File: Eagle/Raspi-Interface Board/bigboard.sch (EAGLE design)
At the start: 25 parts, among them M1 SMALL_SERVO, M2 SMALL_SERVO, M3 SMALL_SERVO, M4 SMALL_SERVO, M5 SMALL_SERVO, U1 ATMEGA328P-AU

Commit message: AVR ISP pins corrected
In the R1 of the board the AVR ISP pins were totally attached to the
wrong. 13 != 3. Double check work done at 4AM next time.
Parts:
- removed IC1, IC2: (no value), RepRapjr:78LXXLM78L05ACZ
- added 3VREG, 5VREG: (no value), SparkFun-Connectors:M03PTH
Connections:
- net 3V: now also 3VREG.1; no longer IC2.OUT
- net 5V: now also 3VREG.3, 5VREG.1; no longer IC1.OUT, IC2.IN
- net A3: now also JP3.4
- net A4: no longer JP3.4
- net ATX: no longer ISP1.MISO
- net D12: now also ISP1.MISO
- net D13: now also ISP1.SCK
- net D3: no longer ISP1.SCK
- net GND: now also 3VREG.2, 5VREG.2; no longer IC1.GND, IC2.GND
- net VIN: now also 5VREG.3; no longer IC1.IN
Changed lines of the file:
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@@
 <part name="M4" library="SparkFun-Electromechanical" deviceset="SMALL_SERVO" device=""/>
 <part name="M5" library="SparkFun-Electromechanical" deviceset="SMALL_SERVO" device=""/>
-<part name="IC1" library="RepRapjr" deviceset="78LXX" device="LM78L05ACZ"/>
-<part name="IC2" library="RepRapjr" deviceset="78LXX" device="LM78L05ACZ"/>
 <part name="Y1" library="SparkFun-FreqCtrl" deviceset="RESONATOR" device="PTH"/>
 <part name="D1" library="SparkFun-LED" deviceset="LED-BLUE" device="0603" value="BLUE"/>
@@
 <part name="JP4" library="SparkFun-Connectors" deviceset="M07" device=""/>
 <part name="ISP1" library="adafruit" deviceset="AVRISP" device="-6"/>
+<part name="5VREG" library="SparkFun-Connectors" deviceset="M03" device="PTH"/>
+<part name="3VREG" library="SparkFun-Connectors" deviceset="M03" device="PTH"/>
 </parts>
 <sheets>
@@
 <instance part="M4" gate="G$1" x="309.88" y="71.12"/>
 <instance part="M5" gate="G$1" x="309.88" y="48.26"/>
-<instance part="IC1" gate="1" x="172.72" y="167.64"/>
-<instance part="IC2" gate="1" x="134.62" y="167.64"/>
 <instance part="Y1" gate="G$1" x="132.08" y="124.46"/>
 <instance part="D1" gate="G$1" x="170.18" y="231.14"/>
@@
 <instance part="JP4" gate="G$1" x="127" y="-43.18"/>
 <instance part="ISP1" gate="G$1" x="162.56" y="93.98"/>
+<instance part="5VREG" gate="G$1" x="109.22" y="177.8"/>
+<instance part="3VREG" gate="G$1" x="109.22" y="160.02"/>
 </instances>
 <busses>
@@
 <wire x1="132.08" y1="-35.56" x2="134.62" y2="-35.56" width="0.1524" layer="91"/>
 </segment>
+<segment>
+<pinref part="ISP1" gate="G$1" pin="MISO"/>
+<wire x1="149.86" y1="96.52" x2="147.32" y2="96.52" width="0.1524" layer="91"/>
+</segment>
 </net>
 <net name="D13" class="0">
@@
 <wire x1="132.08" y1="-33.02" x2="134.62" y2="-33.02" width="0.1524" layer="91"/>
 </segment>
+<segment>
+<pinref part="ISP1" gate="G$1" pin="SCK"/>
+<wire x1="149.86" y1="93.98" x2="147.32" y2="93.98" width="0.1524" layer="91"/>
+</segment>
 </net>
 <net name="XTAL1" class="0">
@@
 <wire x1="134.62" y1="66.04" x2="139.7" y2="66.04" width="0.1524" layer="91"/>
 </segment>
+<segment>
+<pinref part="JP3" gate="G$1" pin="4"/>
+<wire x1="88.9" y1="-40.64" x2="91.44" y2="-40.64" width="0.1524" layer="91"/>
+</segment>
 </net>
 <net name="A4" class="0">
@@
 <pinref part="U1" gate="A" pin="PC4"/>
 <wire x1="134.62" y1="63.5" x2="139.7" y2="63.5" width="0.1524" layer="91"/>
-</segment>
-<segment>
-<pinref part="JP3" gate="G$1" pin="4"/>
-<wire x1="88.9" y1="-40.64" x2="91.44" y2="-40.64" width="0.1524" layer="91"/>
 </segment>
 <segment>
@@
 <junction x="83.82" y="137.16"/>
 </segment>
-<segment>
-<pinref part="ISP1" gate="G$1" pin="MISO"/>
-<wire x1="149.86" y1="96.52" x2="147.32" y2="96.52" width="0.1524" layer="91"/>
-</segment>
 </net>
 <net name="D2" class="0">
@@
 <wire x1="312.42" y1="119.38" x2="317.5" y2="119.38" width="0.1524" layer="91"/>
 </segment>
-<segment>
-<pinref part="ISP1" gate="G$1" pin="SCK"/>
-<wire x1="149.86" y1="93.98" x2="147.32" y2="93.98" width="0.1524" layer="91"/>
-</segment>
 </net>
 <net name="D4" class="0">
@@
 </segment>
 <segment>
-<pinref part="IC1" gate="1" pin="IN"/>
-<wire x1="165.1" y1="167.64" x2="162.56" y2="167.64" width="0.1524" layer="91"/>
+<pinref part="5VREG" gate="G$1" pin="3"/>
+<wire x1="116.84" y1="180.34" x2="119.38" y2="180.34" width="0.1524" layer="91"/>
 </segment>
 </net>
@@
 </segment>
 <segment>
-<pinref part="IC1" gate="1" pin="GND"/>
-<wire x1="172.72" y1="160.02" x2="172.72" y2="157.48" width="0.1524" layer="91"/>
-</segment>
-<segment>
-<pinref part="IC2" gate="1" pin="GND"/>
-<wire x1="134.62" y1="160.02" x2="134.62" y2="157.48" width="0.1524" layer="91"/>
-</segment>
-<segment>
 <pinref part="Y1" gate="G$1" pin="2"/>
 <wire x1="132.08" y1="116.84" x2="132.08" y2="114.3" width="0.1524" layer="91"/>
@@
 <pinref part="ISP1" gate="G$1" pin="GND"/>
 <wire x1="177.8" y1="91.44" x2="180.34" y2="91.44" width="0.1524" layer="91"/>
+</segment>
+<segment>
+<pinref part="5VREG" gate="G$1" pin="2"/>
+<wire x1="116.84" y1="177.8" x2="119.38" y2="177.8" width="0.1524" layer="91"/>
+</segment>
+<segment>
+<pinref part="3VREG" gate="G$1" pin="2"/>
+<wire x1="116.84" y1="160.02" x2="119.38" y2="160.02" width="0.1524" layer="91"/>
 </segment>
 </net>
@@
 </segment>
 <segment>
-<pinref part="IC1" gate="1" pin="OUT"/>
-<wire x1="180.34" y1="167.64" x2="182.88" y2="167.64" width="0.1524" layer="91"/>
-</segment>
-<segment>
-<pinref part="IC2" gate="1" pin="IN"/>
-<wire x1="127" y1="167.64" x2="124.46" y2="167.64" width="0.1524" layer="91"/>
-</segment>
-<segment>
 <pinref part="ISP1" gate="G$1" pin="VCC"/>
 <wire x1="177.8" y1="96.52" x2="180.34" y2="96.52" width="0.1524" layer="91"/>
@@
 <wire x1="38.1" y1="71.12" x2="35.56" y2="71.12" width="0.1524" layer="91"/>
 </segment>
+<segment>
+<pinref part="5VREG" gate="G$1" pin="1"/>
+<wire x1="116.84" y1="175.26" x2="119.38" y2="175.26" width="0.1524" layer="91"/>
+</segment>
+<segment>
+<pinref part="3VREG" gate="G$1" pin="3"/>
+<wire x1="116.84" y1="162.56" x2="119.38" y2="162.56" width="0.1524" layer="91"/>
+</segment>
 </net>
 <net name="3V" class="0">
-<segment>
-<pinref part="IC2" gate="1" pin="OUT"/>
-<wire x1="142.24" y1="167.64" x2="144.78" y2="167.64" width="0.1524" layer="91"/>
-</segment>
 <segment>
 <pinref part="D8" gate="G$1" pin="A"/>
@@
 <wire x1="38.1" y1="66.04" x2="35.56" y2="66.04" width="0.1524" layer="91"/>
 </segment>
-</net>
+<segment>
+<pinref part="3VREG" gate="G$1" pin="1"/>
+<wire x1="116.84" y1="157.48" x2="119.38" y2="157.48" width="0.1524" layer="91"/>
+</segment>
+</net>

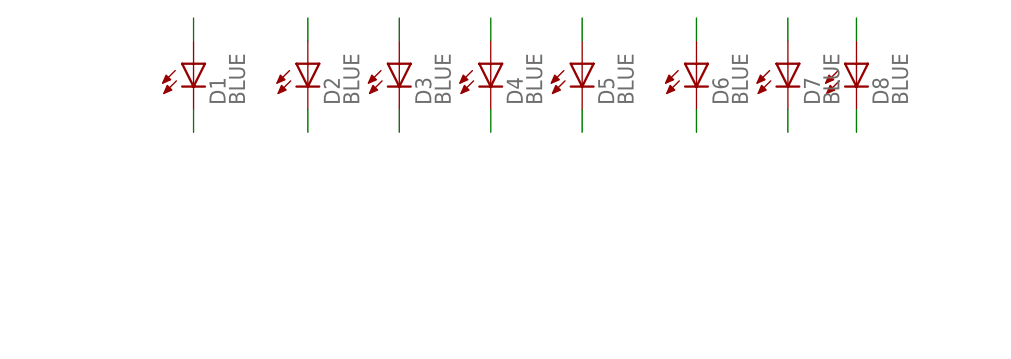
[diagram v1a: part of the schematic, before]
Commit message: Board Update
New Board revision to fix the 3v3 regulator pinout.
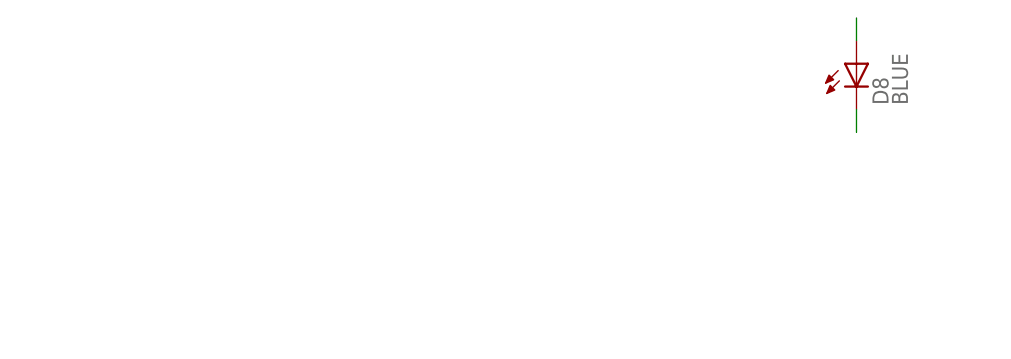
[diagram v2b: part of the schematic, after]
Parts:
- removed D1, D2, D3, D4, D5, D6, D7: BLUE, SparkFun-LED:LED-BLUE0603
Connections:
- net 3V: now also 3VREG.2; no longer 3VREG.1
- net 5V: now also 5VREG.3; no longer 5VREG.1
- net D10: no longer D4.A
- net D11: no longer D5.A
- net D12: no longer D6.A
- net D13: no longer D7.A
- net D7: no longer D1.A
- net D8: no longer D2.A
- net D9: no longer D3.A
- net GND: now also 3VREG.1; no longer 3VREG.2, D1.C, D2.C, D3.C, D4.C, D5.C, D6.C, D7.C
- net VIN: now also 5VREG.1; no longer 5VREG.3
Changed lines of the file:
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@@
 <part name="M5" library="SparkFun-Electromechanical" deviceset="SMALL_SERVO" device=""/>
 <part name="Y1" library="SparkFun-FreqCtrl" deviceset="RESONATOR" device="PTH"/>
-<part name="D1" library="SparkFun-LED" deviceset="LED-BLUE" device="0603" value="BLUE"/>
-<part name="D2" library="SparkFun-LED" deviceset="LED-BLUE" device="0603" value="BLUE"/>
-<part name="D3" library="SparkFun-LED" deviceset="LED-BLUE" device="0603" value="BLUE"/>
-<part name="D4" library="SparkFun-LED" deviceset="LED-BLUE" device="0603" value="BLUE"/>
-<part name="D5" library="SparkFun-LED" deviceset="LED-BLUE" device="0603" value="BLUE"/>
-<part name="D6" library="SparkFun-LED" deviceset="LED-BLUE" device="0603" value="BLUE"/>
-<part name="D7" library="SparkFun-LED" deviceset="LED-BLUE" device="0603" value="BLUE"/>
 <part name="D8" library="SparkFun-LED" deviceset="LED-BLUE" device="0603" value="BLUE"/>
 <part name="JP3" library="SparkFun-Connectors" deviceset="M07" device=""/>
@@
 <instance part="M5" gate="G$1" x="309.88" y="48.26"/>
 <instance part="Y1" gate="G$1" x="132.08" y="124.46"/>
-<instance part="D1" gate="G$1" x="170.18" y="231.14"/>
-<instance part="D2" gate="G$1" x="182.88" y="231.14"/>
-<instance part="D3" gate="G$1" x="193.04" y="231.14"/>
-<instance part="D4" gate="G$1" x="203.2" y="231.14"/>
-<instance part="D5" gate="G$1" x="213.36" y="231.14"/>
-<instance part="D6" gate="G$1" x="226.06" y="231.14"/>
-<instance part="D7" gate="G$1" x="236.22" y="231.14"/>
 <instance part="D8" gate="G$1" x="243.84" y="231.14"/>
 <instance part="JP3" gate="G$1" x="83.82" y="-43.18"/>
@@
 </segment>
 <segment>
-<pinref part="D2" gate="G$1" pin="A"/>
-<wire x1="182.88" y1="233.68" x2="182.88" y2="236.22" width="0.1524" layer="91"/>
-</segment>
-<segment>
 <pinref part="JP4" gate="G$1" pin="2"/>
 <wire x1="132.08" y1="-45.72" x2="134.62" y2="-45.72" width="0.1524" layer="91"/>
@@
 </segment>
 <segment>
-<pinref part="D3" gate="G$1" pin="A"/>
-<wire x1="193.04" y1="233.68" x2="193.04" y2="236.22" width="0.1524" layer="91"/>
-</segment>
-<segment>
 <pinref part="JP4" gate="G$1" pin="3"/>
 <wire x1="132.08" y1="-43.18" x2="134.62" y2="-43.18" width="0.1524" layer="91"/>
@@
 </segment>
 <segment>
-<pinref part="D4" gate="G$1" pin="A"/>
-<wire x1="203.2" y1="233.68" x2="203.2" y2="236.22" width="0.1524" layer="91"/>
-</segment>
-<segment>
 <pinref part="JP4" gate="G$1" pin="4"/>
 <wire x1="132.08" y1="-40.64" x2="134.62" y2="-40.64" width="0.1524" layer="91"/>
@@
 </segment>
 <segment>
-<pinref part="D5" gate="G$1" pin="A"/>
-<wire x1="213.36" y1="233.68" x2="213.36" y2="236.22" width="0.1524" layer="91"/>
-</segment>
-<segment>
 <pinref part="JP4" gate="G$1" pin="5"/>
 <wire x1="132.08" y1="-38.1" x2="134.62" y2="-38.1" width="0.1524" layer="91"/>
@@
 </segment>
 <segment>
-<pinref part="D6" gate="G$1" pin="A"/>
-<wire x1="226.06" y1="233.68" x2="226.06" y2="236.22" width="0.1524" layer="91"/>
-</segment>
-<segment>
 <pinref part="JP4" gate="G$1" pin="6"/>
 <wire x1="132.08" y1="-35.56" x2="134.62" y2="-35.56" width="0.1524" layer="91"/>
@@
 <pinref part="U1" gate="A" pin="PB5"/>
 <wire x1="99.06" y1="38.1" x2="93.98" y2="38.1" width="0.1524" layer="91"/>
-</segment>
-<segment>
-<pinref part="D7" gate="G$1" pin="A"/>
-<wire x1="236.22" y1="233.68" x2="236.22" y2="236.22" width="0.1524" layer="91"/>
 </segment>
 <segment>
@@
 </segment>
 <segment>
-<pinref part="D1" gate="G$1" pin="A"/>
-<wire x1="170.18" y1="233.68" x2="170.18" y2="236.22" width="0.1524" layer="91"/>
-</segment>
-<segment>
 <pinref part="JP4" gate="G$1" pin="1"/>
 <wire x1="132.08" y1="-48.26" x2="134.62" y2="-48.26" width="0.1524" layer="91"/>
@@
 </segment>
 <segment>
-<pinref part="5VREG" gate="G$1" pin="3"/>
-<wire x1="116.84" y1="180.34" x2="119.38" y2="180.34" width="0.1524" layer="91"/>
+<pinref part="5VREG" gate="G$1" pin="1"/>
+<wire x1="116.84" y1="175.26" x2="119.38" y2="175.26" width="0.1524" layer="91"/>
 </segment>
 </net>
@@
 </segment>
 <segment>
-<pinref part="D1" gate="G$1" pin="C"/>
-<wire x1="170.18" y1="226.06" x2="170.18" y2="223.52" width="0.1524" layer="91"/>
-</segment>
-<segment>
-<pinref part="D2" gate="G$1" pin="C"/>
-<wire x1="182.88" y1="226.06" x2="182.88" y2="223.52" width="0.1524" layer="91"/>
-</segment>
-<segment>
-<pinref part="D3" gate="G$1" pin="C"/>
-<wire x1="193.04" y1="226.06" x2="193.04" y2="223.52" width="0.1524" layer="91"/>
-</segment>
-<segment>
-<pinref part="D4" gate="G$1" pin="C"/>
-<wire x1="203.2" y1="226.06" x2="203.2" y2="223.52" width="0.1524" layer="91"/>
-</segment>
-<segment>
-<pinref part="D5" gate="G$1" pin="C"/>
-<wire x1="213.36" y1="226.06" x2="213.36" y2="223.52" width="0.1524" layer="91"/>
-</segment>
-<segment>
-<pinref part="D6" gate="G$1" pin="C"/>
-<wire x1="226.06" y1="226.06" x2="226.06" y2="223.52" width="0.1524" layer="91"/>
-</segment>
-<segment>
-<pinref part="D7" gate="G$1" pin="C"/>
-<wire x1="236.22" y1="226.06" x2="236.22" y2="223.52" width="0.1524" layer="91"/>
-</segment>
-<segment>
 <pinref part="D8" gate="G$1" pin="C"/>
 <wire x1="243.84" y1="226.06" x2="243.84" y2="223.52" width="0.1524" layer="91"/>
@@
 </segment>
 <segment>
-<pinref part="3VREG" gate="G$1" pin="2"/>
-<wire x1="116.84" y1="160.02" x2="119.38" y2="160.02" width="0.1524" layer="91"/>
+<pinref part="3VREG" gate="G$1" pin="1"/>
+<wire x1="116.84" y1="157.48" x2="119.38" y2="157.48" width="0.1524" layer="91"/>
 </segment>
 </net>
@@
 </segment>
 <segment>
-<pinref part="5VREG" gate="G$1" pin="1"/>
-<wire x1="116.84" y1="175.26" x2="119.38" y2="175.26" width="0.1524" layer="91"/>
-</segment>
-<segment>
 <pinref part="3VREG" gate="G$1" pin="3"/>
 <wire x1="116.84" y1="162.56" x2="119.38" y2="162.56" width="0.1524" layer="91"/>
 </segment>
+<segment>
+<pinref part="5VREG" gate="G$1" pin="3"/>
+<wire x1="116.84" y1="180.34" x2="119.38" y2="180.34" width="0.1524" layer="91"/>
+</segment>
 </net>
 <net name="3V" class="0">
@@
 </segment>
 <segment>
-<pinref part="3VREG" gate="G$1" pin="1"/>
-<wire x1="116.84" y1="157.48" x2="119.38" y2="157.48" width="0.1524" layer="91"/>
-</segment>
-</net>
+<pinref part="3VREG" gate="G$1" pin="2"/>
+<wire x1="116.84" y1="160.02" x2="119.38" y2="160.02" width="0.1524" layer="91"/>
+</segment>
+</net>
